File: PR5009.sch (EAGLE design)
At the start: 47 parts

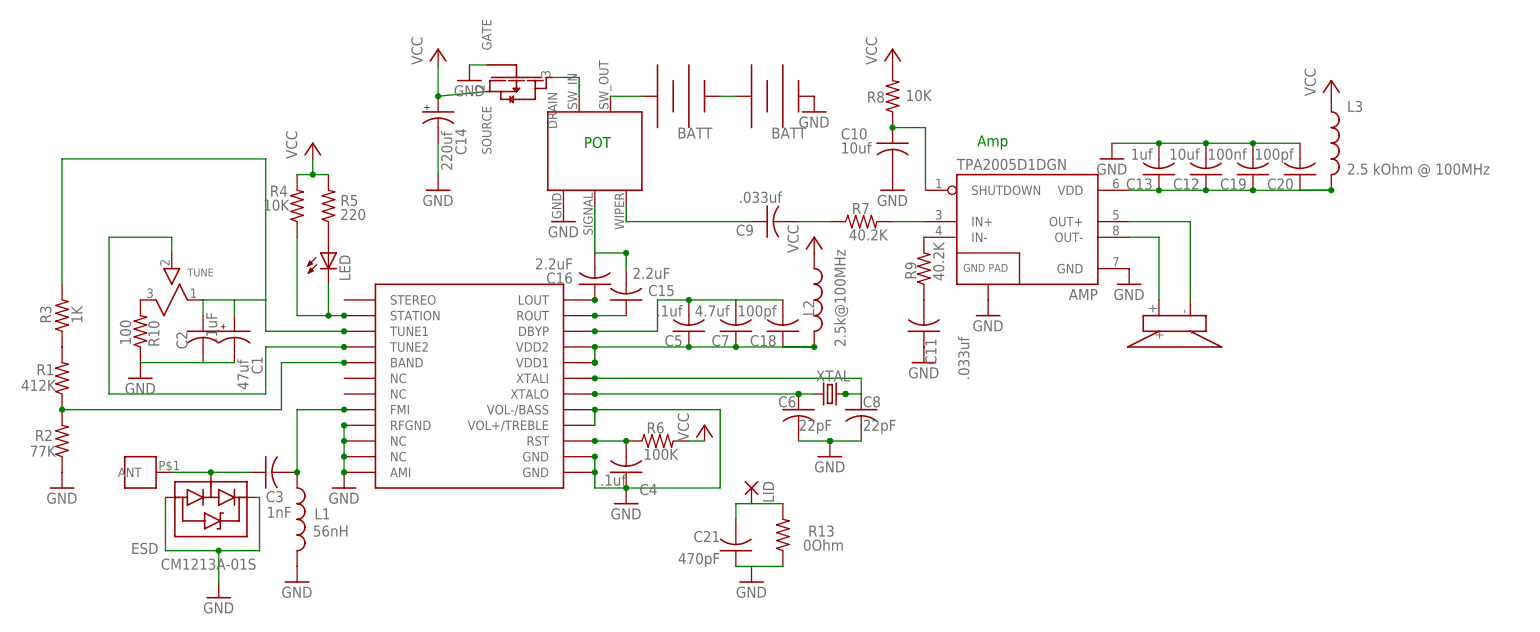
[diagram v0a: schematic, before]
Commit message: Updates and Fixes
Small changes, clearing Osh Park design rules
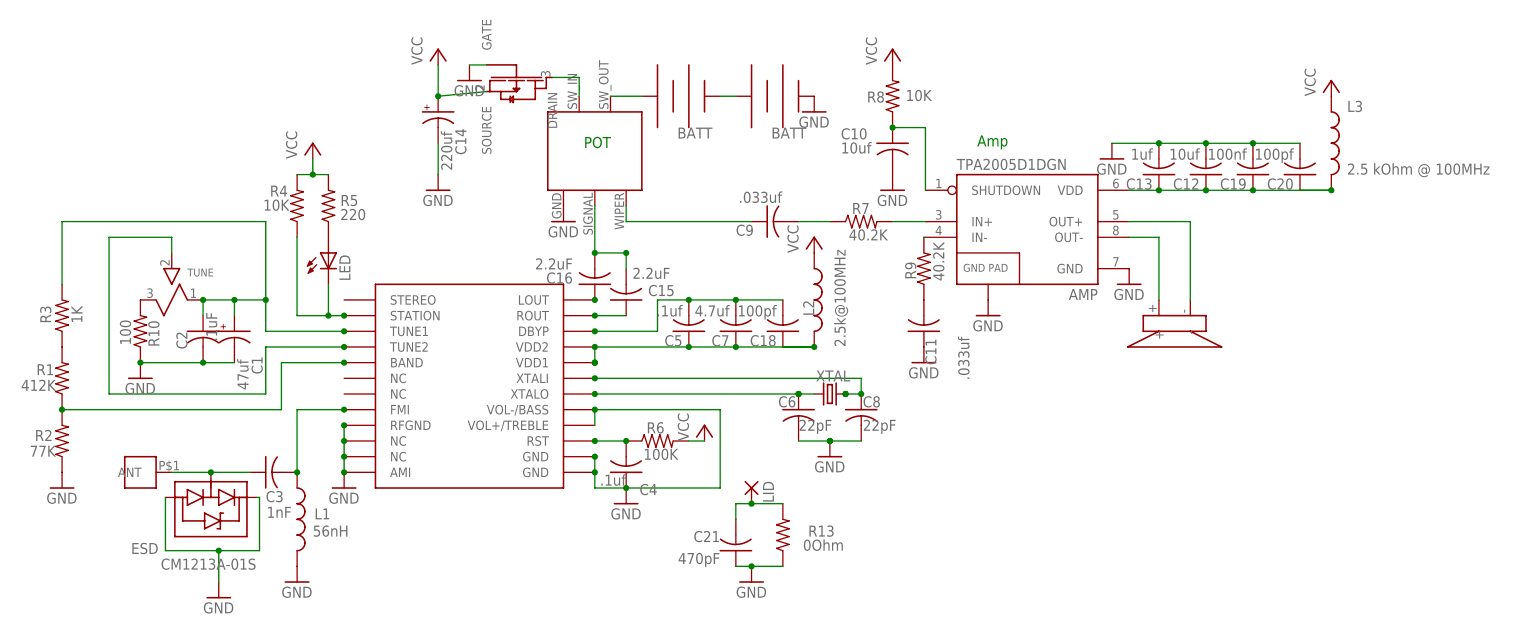
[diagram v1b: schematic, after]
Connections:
- removed net N$35: R3.2
- net N$22: now also R3.2
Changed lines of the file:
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@@
 <?xml version="1.0" encoding="utf-8"?>
 <!DOCTYPE eagle SYSTEM "eagle.dtd">
-<eagle version="6.6.0">
+<eagle version="6.4">
 <drawing>
 <settings>
@@
 <wire x1="-5.08" y1="76.2" x2="-10.16" y2="76.2" width="0.1524" layer="91"/>
 <wire x1="-10.16" y1="76.2" x2="-20.32" y2="76.2" width="0.1524" layer="91"/>
+<junction x="-20.32" y="76.2"/>
+<junction x="-10.16" y="76.2"/>
 </segment>
 <segment>
@@
 <pinref part="R13" gate="G$1" pin="1"/>
 <wire x1="83.82" y1="43.18" x2="78.74" y2="43.18" width="0.1524" layer="91"/>
+<junction x="78.74" y="43.18"/>
 </segment>
 <segment>
@@
 <pinref part="U$4" gate="G$1" pin="DBYP"/>
 <junction x="53.34" y="81.28"/>
+<junction x="76.2" y="86.36"/>
 </segment>
 </net>
@@
 <junction x="53.34" y="73.66"/>
 <wire x1="93.98" y1="71.12" x2="96.52" y2="71.12" width="0.1524" layer="91"/>
+<junction x="96.52" y="71.12"/>
 </segment>
 </net>
@@
 <pinref part="C15" gate="G$1" pin="2"/>
 <pinref part="C16" gate="G$1" pin="2"/>
+<junction x="53.34" y="93.98"/>
 </segment>
 </net>
@@
 <pinref part="C2" gate="G$1" pin="1"/>
 <wire x1="-10.16" y1="83.82" x2="-10.16" y2="86.36" width="0.1524" layer="91"/>
+<pinref part="R3" gate="G$1" pin="2"/>
+<wire x1="-33.02" y1="88.9" x2="-33.02" y2="99.06" width="0.1524" layer="91"/>
+<wire x1="-33.02" y1="99.06" x2="0" y2="99.06" width="0.1524" layer="91"/>
+<wire x1="0" y1="99.06" x2="0" y2="86.36" width="0.1524" layer="91"/>
+<junction x="0" y="86.36"/>
+<junction x="-5.08" y="86.36"/>
+<junction x="-10.16" y="86.36"/>
 </segment>
 </net>
@@
 </segment>
 </net>
-<net name="N$21" class="0">
-<segment>
-<pinref part="U$1" gate="BATT" pin="POS"/>
-<pinref part="U$5" gate="G$1" pin="SW_OUT"/>
-<wire x1="60.96" y1="119.38" x2="55.88" y2="119.38" width="0.1524" layer="91"/>
-</segment>
-</net>
 <net name="N$30" class="0">
 <segment>
@@
 <wire x1="50.8" y1="119.38" x2="50.8" y2="122.428" width="0.1524" layer="91"/>
 <wire x1="50.8" y1="122.428" x2="46.482" y2="122.428" width="0.1524" layer="91"/>
-</segment>
-</net>
-<net name="N$35" class="0">
-<segment>
-<pinref part="R3" gate="G$1" pin="2"/>
-<wire x1="-33.02" y1="88.9" x2="-33.02" y2="109.22" width="0.1524" layer="91"/>
-<wire x1="-33.02" y1="109.22" x2="0" y2="109.22" width="0.1524" layer="91"/>
-<wire x1="0" y1="109.22" x2="0" y2="86.36" width="0.1524" layer="91"/>
 </segment>
 </net>
@@
 <pinref part="R13" gate="G$1" pin="2"/>
 <wire x1="78.74" y1="53.34" x2="83.82" y2="53.34" width="0.1524" layer="91"/>
+<junction x="78.74" y="53.34"/>
+</segment>
+</net>
+<net name="N$21" class="0">
+<segment>
+<pinref part="U$1" gate="BATT" pin="POS"/>
+<pinref part="U$5" gate="G$1" pin="SW_OUT"/>
+<wire x1="60.96" y1="119.38" x2="55.88" y2="119.38" width="0.1524" layer="91"/>
 </segment>
 </net>
@@
 </sheet>
 </sheets>
+<errors>
+</errors>
 </schematic>
 </drawing>
